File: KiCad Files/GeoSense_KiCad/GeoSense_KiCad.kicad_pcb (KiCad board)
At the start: 2 copper layers, 120.5 x 97 mm, 168 parts, among them J0 Conn_01x04_Pin, J1 Conn_01x04_Pin, J10 Conn_01x01_Socket, J11 Conn_01x01_Socket, J12 Conn_01x01_Socket, J13 Conn_01x01_Socket, J14 Conn_01x04_Pin, J15 Conn_01x02_Pin, J2 Conn_01x04_Pin, J3 Conn_01x04_Pin, J4 Conn_01x04_Pin, J5 Conn_01x04_Pin, J6 Conn_01x04_Pin, J7 Conn_01x04_Pin, J8 Conn_01x04_Pin, J9 Conn_01x04_Pin, U1 LM324, U1.1 LM334Z, U1.2 LM334Z, U2 LM324, U2.1 LM334Z, U2.2 LM334Z, U3 LM324, U3.1 LM334Z, U3.2 LM334Z, U4 LM324, U4.1 LM334Z, U4.2 LM334Z, U5 LM324, U5.1 LM334Z, U5.2 LM334Z, U6 LM324, U6.1 LM334Z, U6.2 LM334Z, U7 LM324, U7.1 LM334Z, U7.2 LM334Z, U8 LM324, U8.1 LM334Z, U8.2 LM334Z

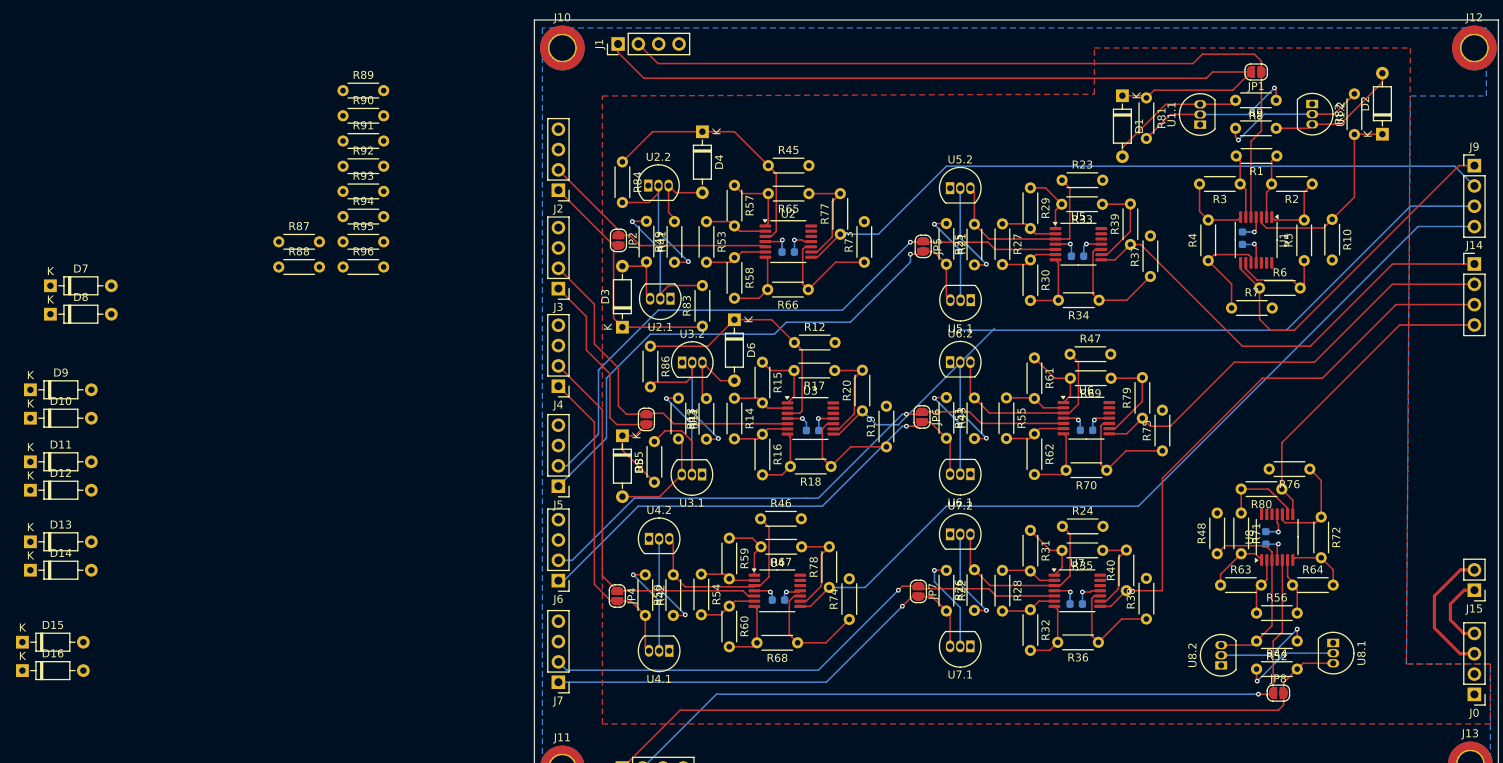
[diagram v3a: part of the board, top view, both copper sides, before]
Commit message: added diodes and resistors to pcb
silkscreen needs fixing
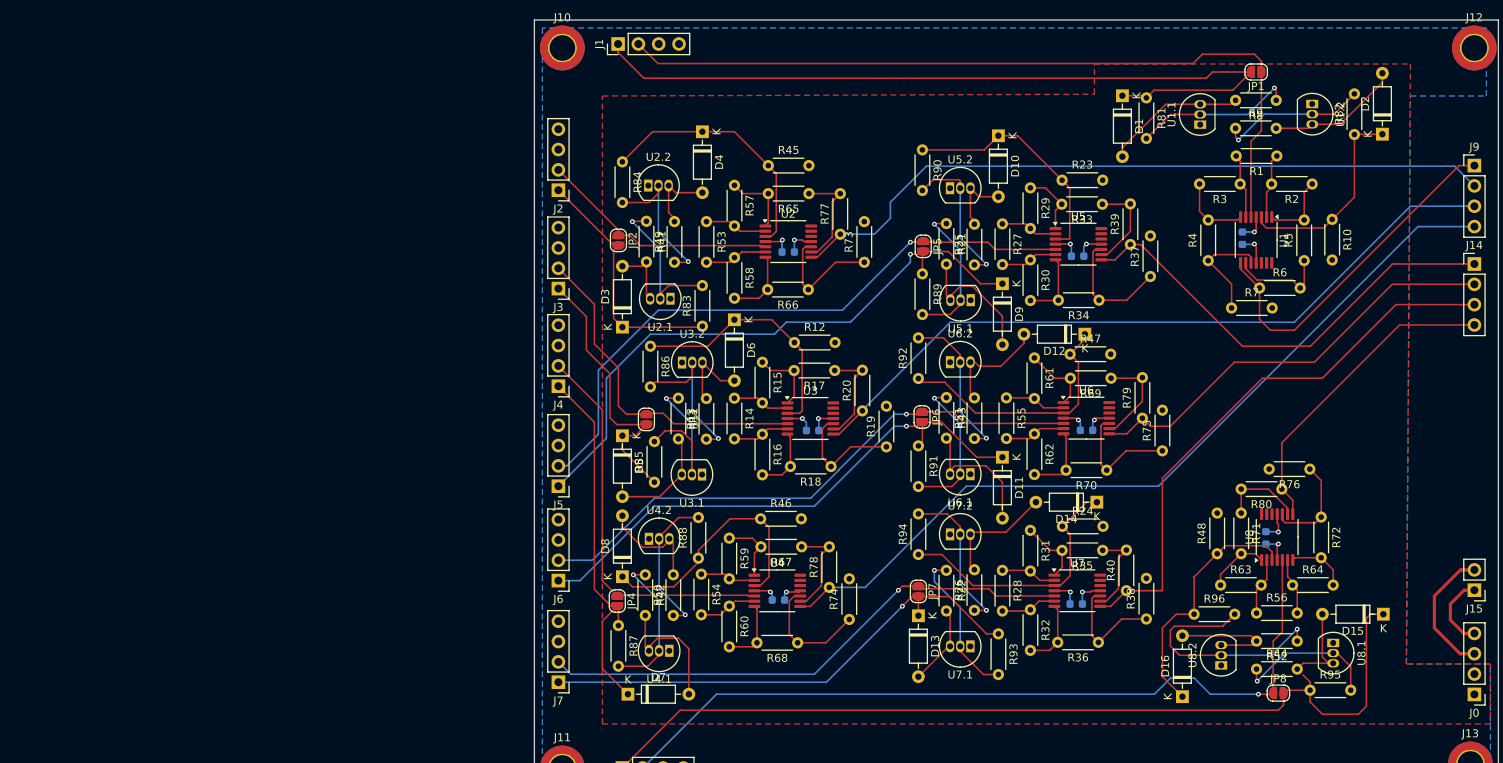
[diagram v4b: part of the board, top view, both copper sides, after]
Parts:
- moved D15 170.2 mm to (191.1, 119.0), turned to 180 degrees
- moved D16 145.0 mm to (166.0, 129.3), turned to 90 degrees
- moved D14 133.6 mm to (155.3, 105.0), turned to 180 degrees
- moved D12 133.2 mm to (153.8, 84.0), turned to 180 degrees
- moved R95 133.2 mm to (182.0, 128.5)
- moved D10 126.0 mm to (143.0, 59.2), turned to -90 degrees
- moved D9 122.2 mm to (143.5, 77.7), turned to -90 degrees
- moved D11 121.5 mm to (143.5, 99.4), turned to -90 degrees
- moved R96 114.9 mm to (167.5, 119.0)
- moved D13 111.4 mm to (133.0, 119.2), turned to -90 degrees
- moved R93 98.8 mm to (143.0, 121.5), turned to -90 degrees
- moved D7 88.4 mm to (96.7, 129.0)
- moved R94 83.4 mm to (133.0, 111.5), turned to 90 degrees
- moved R91 81.4 mm to (133.0, 98.0), turned to -90 degrees
- moved D8 78.7 mm to (96.0, 114.3), turned to 90 degrees
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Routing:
- net T8.1 In: track 96.1 -> 116.0 mm
- net Net-(R52-Pad1): track 12.4 -> 30.0 mm
- net Net-(D9-A): track 0.00 -> 17.3 mm
- net Net-(D11-A): track 0.00 -> 17.3 mm
- net Net-(D7-A): track 0.00 -> 16.8 mm
- net Net-(D16-A): track 0.00 -> 14.2 mm
- net Net-(D14-A): track 0.00 -> 14.1 mm
- net Net-(D8-A): track 0.00 -> 13.8 mm
- net Net-(D12-A): track 0.00 -> 13.7 mm
- net Net-(D15-A): track 0.00 -> 11.8 mm
- net Net-(D13-A): track 0.00 -> 9.74 mm
- net T7.C: track 24.5 -> 33.2 mm
- net Net-(D10-A): track 0.00 -> 8.29 mm
- net T8.C: track 24.2 -> 31.6 mm
- net T4.1 In: track 39.2 -> 46.6 mm
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
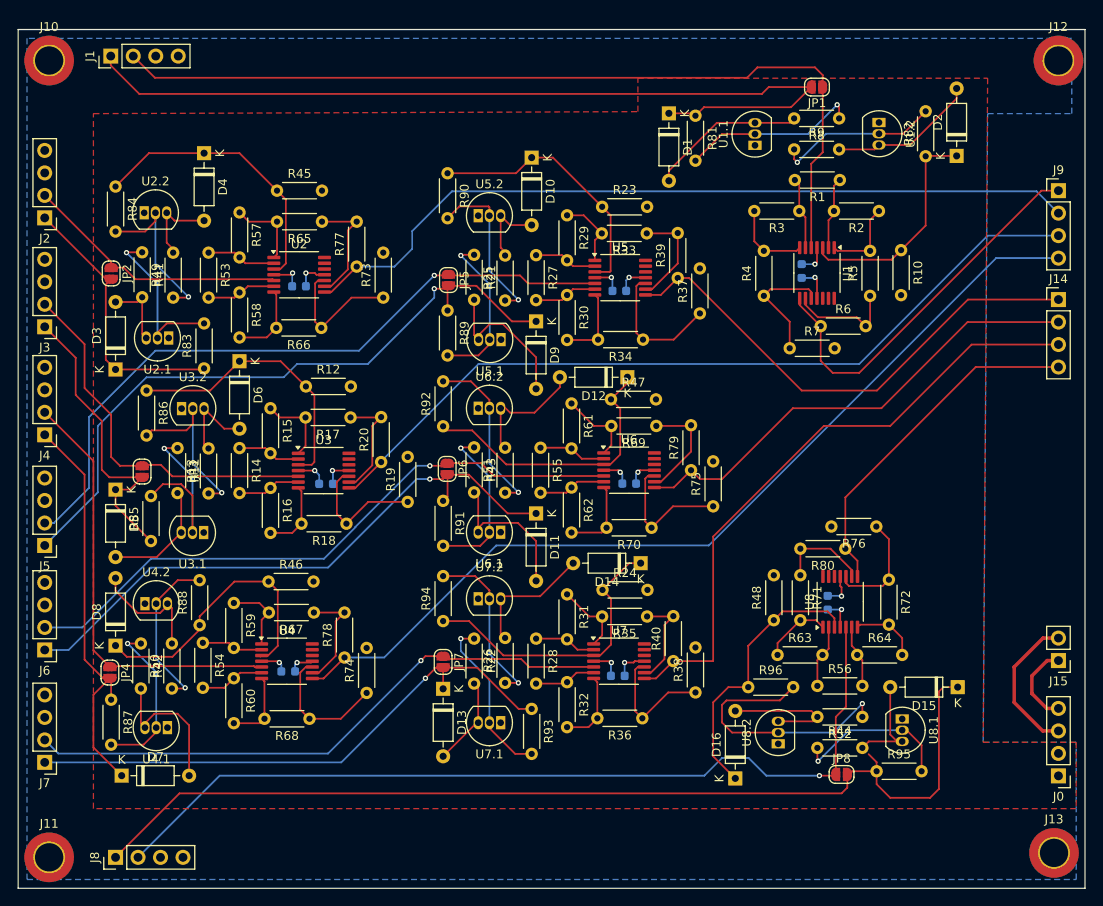
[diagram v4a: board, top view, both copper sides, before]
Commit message: finished the silkscreen edits
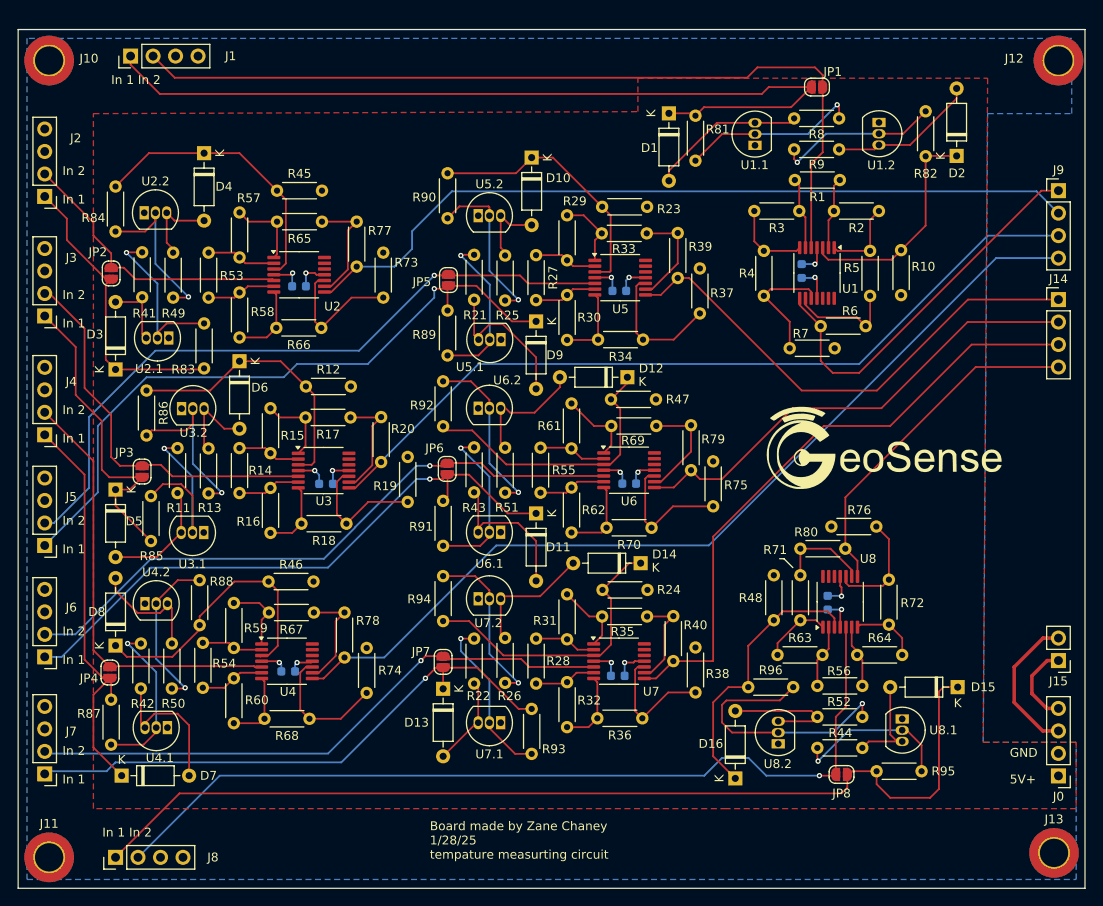
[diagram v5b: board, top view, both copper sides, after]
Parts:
- added G***: LOGO, Logo:GeoSenseGFnLogo, F.Cu at (183.0, 92.0)
- moved J2 2.42 mm to (88.0, 63.6)
- moved J1 2.24 mm to (97.7, 47.7)
- moved J7 1.30 mm to (88.0, 128.8)
- moved J3 1.22 mm to (88.0, 77.1)
- moved J6 0.78 mm to (88.0, 115.6)
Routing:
- net T2.2 In: track 30.2 -> 32.7 mm
- net T2.1 In: track 31.5 -> 33.9 mm
- net T8.1 In: track 116.0 -> 113.7 mm
- net T1.1 In: track 99.3 -> 97.1 mm
- net T1.2 In: track 99.8 -> 97.5 mm
- net T3.2 In: track 41.9 -> 43.5 mm
- net T3.1 In: track 34.8 -> 36.0 mm
- net T7.1 In: track 63.8 -> 64.3 mm
- net T7.2 In: track 67.7 -> 67.2 mm
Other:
- board text added: "5V+"
- board text added: "Board made by Zane Chaney 1/28/25 tempature measurting circuit"
- board text added: "GND"
- board text added: "In 1 In 2"
- board text added: "In 2 In 1"
- board text added: "O1 O2 O3 O4 O5 O6 O7 O8"

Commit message: updated to kicad 9.0.1
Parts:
- removed the G*** at (183.0, 92.0)
- added G***: LOGO, Logo kicad:GeoSenseGFnLogo, F.Cu at (183.5, 92.5)
